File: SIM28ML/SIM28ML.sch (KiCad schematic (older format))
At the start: 26 parts, among them IC1 SIM28M, J1 Conn_01x05, J2 Conn_01x05, U2 AP7365-W-7

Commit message: Part Numbers Added
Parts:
- AE1: Part (none) -> C88374
- BT1: Part (none) -> C238097
- C1: Part (none) -> C87998
- C2, C6: Part (none) -> C42998
- C3, C4: Part (none) -> C396719
- IC1: Description GPS Receiver -> (none); Height 2 -> (none); Manufacturer_Name SIMCOM -> (none); Manufacturer_Part_Number SIM28M -> (none); Part (none) -> OTTO
- L1: Part (none) -> C142204
- R1, R2: Part (none) -> C245184
- R3: Part (none) -> C99198
- R4: Part (none) -> C269698
- R5: Part (none) -> C176153
- R7: Part (none) -> C163436
- R8: Part (none) -> C103426
- U2: Part (none) -> C264087
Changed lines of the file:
@@
 EESchema Schematic File Version 4
-LIBS:SIM28M-cache
+LIBS:SIM28ML-cache
 EELAYER 29 0
 EELAYER END
@@
 F 2 "Package_TO_SOT_SMD:SOT-23-5" H 2450 1675 50  0001 C CNN
 F 3 "https://www.diodes.com/assets/Datasheets/AP2127.pdf" H 2450 1450 50  0001 C CNN
+F 4 "C264087" H 2450 1350 50  0001 C CNN "Part"
 	1    2450 1350
 	1    0    0    -1
@@
 F 2 "Resistor_SMD:R_0603_1608Metric" V 3040 1240 50  0001 C CNN
 F 3 "~" H 3000 1250 50  0001 C CNN
+F 4 "C163436" V 3000 1250 50  0001 C CNN "Part"
 	1    3000 1250
 	0    -1   -1   0
@@
 F 2 "Resistor_SMD:R_0603_1608Metric" V 3240 1540 50  0001 C CNN
 F 3 "~" H 3200 1550 50  0001 C CNN
+F 4 "C103426" H 3200 1550 50  0001 C CNN "Part"
 	1    3200 1550
 	-1   0    0    1
@@
 F 2 "SirBoardLibrary:SIM28M" H 4150 2750 50  0001 L CNN
 F 3 "http://simcomm2m.com/UploadFile/TechnicalFile/SIM28M_Hardware%20Design_V1.00.pdf" H 4150 2650 50  0001 L CNN
-F 4 "GPS Receiver" H 4150 2550 50  0001 L CNN "Description"
-F 5 "2" H 4150 2450 50  0001 L CNN "Height"
-F 6 "SIMCOM" H 4150 2350 50  0001 L CNN "Manufacturer_Name"
-F 7 "SIM28M" H 4150 2250 50  0001 L CNN "Manufacturer_Part_Number"
-F 8 "" H 4150 2150 50  0001 L CNN "Mouser Part Number"
-F 9 "" H 4150 2050 50  0001 L CNN "Mouser Price/Stock"
-F 10 "" H 4150 1950 50  0001 L CNN "RS Part Number"
-F 11 "" H 4150 1850 50  0001 L CNN "RS Price/Stock"
+F 4 "OTTO" H 2800 2650 50  0001 C CNN "Part"
 	1    2800 2650
 	1    0    0    -1
@@
 F 2 "Resistor_SMD:R_0603_1608Metric" V 2290 2840 50  0001 C CNN
 F 3 "~" H 2250 2850 50  0001 C CNN
+F 4 "C245184" V 2250 2850 50  0001 C CNN "Part"
 	1    2250 2850
 	0    -1   1    0
@@
 F 2 "Resistor_SMD:R_0603_1608Metric" V 5140 3340 50  0001 C CNN
 F 3 "~" H 5100 3350 50  0001 C CNN
+F 4 "C269698" V 5100 3350 50  0001 C CNN "Part"
 	1    5100 3350
 	0    -1   1    0
@@
 F 2 "Resistor_SMD:R_0603_1608Metric" V 5140 3040 50  0001 C CNN
 F 3 "~" H 5100 3050 50  0001 C CNN
+F 4 "C176153" V 5100 3050 50  0001 C CNN "Part"
 	1    5100 3050
 	0    -1   1    0
@@
 F 2 "Resistor_SMD:R_0603_1608Metric" V 2290 2740 50  0001 C CNN
 F 3 "~" H 2250 2750 50  0001 C CNN
+F 4 "C245184" V 2250 2750 50  0001 C CNN "Part"
 	1    2250 2750
 	0    -1   -1   0
@@
 F 2 "Battery:BatteryHolder_Keystone_3000_1x12mm" V 2650 3810 50  0001 C CNN
 F 3 "~" V 2650 3810 50  0001 C CNN
+F 4 "C238097" H 2650 3750 50  0001 C CNN "Part"
 	1    2650 3750
 	-1   0    0    -1
@@
 F 2 "Capacitor_SMD:C_0805_2012Metric" H 1488 3450 50  0001 C CNN
 F 3 "~" H 1450 3600 50  0001 C CNN
+F 4 "C87998" H 1450 3600 50  0001 C CNN "Part"
 	1    1450 3600
 	1    0    0    -1
@@
 F 2 "Capacitor_SMD:C_0603_1608Metric" H 1838 3450 50  0001 C CNN
 F 3 "~" H 1800 3600 50  0001 C CNN
+F 4 "C42998" H 1800 3600 50  0001 C CNN "Part"
 	1    1800 3600
 	1    0    0    -1
@@
 F 2 "Inductor_SMD:L_0603_1608Metric" H 5650 3050 50  0001 C CNN
 F 3 "~" H 5650 3050 50  0001 C CNN
+F 4 "C142204" V 5650 3050 50  0001 C CNN "Part"
 	1    5650 3050
 	0    1    -1   0
@@
 F 2 "Capacitor_SMD:C_0603_1608Metric" H 4838 2650 50  0001 C CNN
 F 3 "~" H 4800 2800 50  0001 C CNN
+F 4 "C42998" H 4800 2800 50  0001 C CNN "Part"
 	1    4800 2800
 	1    0    0    1
@@
 F 2 "Connector_Coaxial:U.FL_Hirose_U.FL-R-SMT-1_Vertical" H 6200 2950 50  0001 C CNN
 F 3 "~" H 6200 2950 50  0001 C CNN
+F 4 "C88374" H 6200 2850 50  0001 C CNN "Part"
 	1    6200 2850
 	1    0    0    -1
@@
 F 2 "Capacitor_SMD:C_0805_2012Metric" H 1588 1400 50  0001 C CNN
 F 3 "~" H 1550 1550 50  0001 C CNN
+F 4 "C396719" H 1550 1550 50  0001 C CNN "Part"
 	1    1550 1550
 	1    0    0    -1
@@
 F 2 "Resistor_SMD:R_0603_1608Metric" V 1890 1340 50  0001 C CNN
 F 3 "~" H 1850 1350 50  0001 C CNN
+F 4 "C99198" V 1850 1350 50  0001 C CNN "Part"
 	1    1850 1350
 	0    -1   1    0
@@
 F 2 "Capacitor_SMD:C_0805_2012Metric" H 3488 1400 50  0001 C CNN
 F 3 "~" H 3450 1550 50  0001 C CNN
+F 4 "C396719" H 3450 1550 50  0001 C CNN "Part"
 	1    3450 1550
 	1    0    0    -1

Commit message: Power LED added
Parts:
- removed R7: 68K, Resistor_SMD:R_0603_1608Metric, symbol Device:R_US
- removed R8: 22K, Resistor_SMD:R_0603_1608Metric, symbol Device:R_US
- removed U2: AP7365-W-7, Package_TO_SOT_SMD:SOT-23-5, symbol Regulator_Linear:AP2127K-ADJ
- added D1: LED, LED_SMD:LED_0603_1608Metric, symbol Device:LED
- added JP2: SolderJumper_2_Bridged, Jumper:SolderJumper-2_P1.3mm_Bridged_RoundedPad1.0x1.5mm, symbol Jumper:SolderJumper_2_Bridged
- added R6: 680E, Resistor_SMD:R_0603_1608Metric, symbol Device:R_US
- added U1: AP2127K-3.3, Package_TO_SOT_SMD:SOT-23-5, symbol Regulator_Linear:AP2127K-3.3
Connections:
- wire segments 85 -> 82
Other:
- moved on the sheet: C3, C4, R3
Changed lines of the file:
@@
 Comment4 ""
 $EndDescr
-Text GLabel 3600 1100 2    50   Input ~ 0
+Text GLabel 3300 925  2    50   Input ~ 0
 3V3
 Wire Wire Line
-	1550 1400 1550 1350
-Wire Wire Line
-	1550 1700 1550 1850
+	1275 1300 1275 1025
+Wire Wire Line
+	1275 1600 1275 1925
 $Comp
 L power:GND #PWR0103
 U 1 1 5DFA7870
-P 2450 1950
-F 0 "#PWR0103" H 2450 1700 50  0001 C CNN
-F 1 "GND" H 2455 1777 50  0000 C CNN
-F 2 "" H 2450 1950 50  0001 C CNN
-F 3 "" H 2450 1950 50  0001 C CNN
-	1    2450 1950
-	1    0    0    -1
-$EndComp
-$Comp
-L Regulator_Linear:AP2127K-ADJ U2
-U 1 1 5E2BA0AD
-P 2450 1350
-F 0 "U2" H 2450 1690 50  0000 C CNN
-F 1 "AP7365-W-7" H 2450 1600 50  0000 C CNN
-F 2 "Package_TO_SOT_SMD:SOT-23-5" H 2450 1675 50  0001 C CNN
-F 3 "https://www.diodes.com/assets/Datasheets/AP2127.pdf" H 2450 1450 50  0001 C CNN
-F 4 "C264087" H 2450 1350 50  0001 C CNN "Part"
-	1    2450 1350
-	1    0    0    -1
-$EndComp
-$Comp
-L Device:R_US R7
-U 1 1 5E34715F
-P 3000 1250
-F 0 "R7" V 3068 1296 50  0000 L CNN
-F 1 "68K" V 3068 1205 50  0000 R CNN
-F 2 "Resistor_SMD:R_0603_1608Metric" V 3040 1240 50  0001 C CNN
-F 3 "~" H 3000 1250 50  0001 C CNN
-F 4 "C163436" V 3000 1250 50  0001 C CNN "Part"
-	1    3000 1250
-	0    -1   -1   0
-$EndComp
-$Comp
-L Device:R_US R8
-U 1 1 5E35753D
-P 3200 1550
-F 0 "R8" H 3300 1500 50  0000 L CNN
-F 1 "22K" H 3400 1600 50  0000 R CNN
-F 2 "Resistor_SMD:R_0603_1608Metric" V 3240 1540 50  0001 C CNN
-F 3 "~" H 3200 1550 50  0001 C CNN
-F 4 "C103426" H 3200 1550 50  0001 C CNN "Part"
-	1    3200 1550
-	-1   0    0    1
-$EndComp
-Wire Wire Line
-	3200 1350 2750 1350
-Wire Wire Line
-	3150 1250 3200 1250
-Wire Wire Line
-	3200 1400 3200 1350
+P 2175 2025
+F 0 "#PWR0103" H 2175 1775 50  0001 C CNN
+F 1 "GND" H 2180 1852 50  0000 C CNN
+F 2 "" H 2175 2025 50  0001 C CNN
+F 3 "" H 2175 2025 50  0001 C CNN
+	1    2175 2025
+	1    0    0    -1
+$EndComp
 $Comp
 L SIM28M:SIM28M IC1
@@
 Connection ~ 1450 3350
 Wire Wire Line
-	1550 1850 2450 1850
-Wire Wire Line
-	3200 1700 3200 1850
-Wire Wire Line
-	3200 1350 3200 1250
-Connection ~ 3200 1350
-Wire Wire Line
-	2750 1250 2800 1250
-Wire Wire Line
-	2800 1250 2800 1100
-Connection ~ 2800 1250
-Wire Wire Line
-	2800 1250 2850 1250
-Wire Wire Line
-	2800 1100 3450 1100
+	1275 1925 2175 1925
 $Comp
 L Device:C C3
 U 1 1 5DCB3070
-P 1550 1550
-F 0 "C3" H 1665 1595 50  0000 L CNN
-F 1 "1uF" H 1665 1505 50  0000 L CNN
-F 2 "Capacitor_SMD:C_0805_2012Metric" H 1588 1400 50  0001 C CNN
-F 3 "~" H 1550 1550 50  0001 C CNN
-F 4 "C396719" H 1550 1550 50  0001 C CNN "Part"
-	1    1550 1550
-	1    0    0    -1
-$EndComp
-Wire Wire Line
-	3450 1400 3450 1100
-Connection ~ 3450 1100
-Wire Wire Line
-	3450 1100 3600 1100
-Wire Wire Line
-	3450 1700 3450 1850
-Wire Wire Line
-	3450 1850 3200 1850
-Connection ~ 3200 1850
-Text GLabel 1300 1250 0    50   Input ~ 0
+P 1275 1450
+F 0 "C3" H 1390 1495 50  0000 L CNN
+F 1 "1uF" H 1390 1405 50  0000 L CNN
+F 2 "Capacitor_SMD:C_0805_2012Metric" H 1313 1300 50  0001 C CNN
+F 3 "~" H 1275 1450 50  0001 C CNN
+F 4 "C396719" H 1275 1450 50  0001 C CNN "Part"
+	1    1275 1450
+	1    0    0    -1
+$EndComp
+Text GLabel 1025 925  0    50   Input ~ 0
 VIN
 Wire Wire Line
-	1300 1250 1550 1250
-Connection ~ 1550 1250
+	1025 925  1275 925
+Connection ~ 1275 925
 Text GLabel 4500 2000 0    50   Input ~ 0
 3V3
@@
 VIN
 Wire Wire Line
-	1550 1250 2150 1250
+	1275 925  1875 925
 $Comp
 L Device:R_US R3
 U 1 1 5DCC87E2
-P 1850 1350
-F 0 "R3" V 1918 1396 50  0000 L CNN
-F 1 "10K" V 1918 1305 50  0000 R CNN
-F 2 "Resistor_SMD:R_0603_1608Metric" V 1890 1340 50  0001 C CNN
-F 3 "~" H 1850 1350 50  0001 C CNN
-F 4 "C99198" V 1850 1350 50  0001 C CNN "Part"
-	1    1850 1350
+P 1575 1025
+F 0 "R3" V 1643 1071 50  0000 L CNN
+F 1 "10K" V 1643 980 50  0000 R CNN
+F 2 "Resistor_SMD:R_0603_1608Metric" V 1615 1015 50  0001 C CNN
+F 3 "~" H 1575 1025 50  0001 C CNN
+F 4 "C99198" V 1575 1025 50  0001 C CNN "Part"
+	1    1575 1025
 	0    -1   1    0
 $EndComp
 Wire Wire Line
-	2000 1350 2100 1350
-Wire Wire Line
-	1700 1350 1550 1350
-Connection ~ 1550 1350
-Wire Wire Line
-	1550 1350 1550 1250
-Text GLabel 2050 1550 0    50   Input ~ 0
-EN
-Wire Wire Line
-	2050 1550 2100 1550
-Wire Wire Line
-	2100 1550 2100 1350
-Connection ~ 2100 1350
-Wire Wire Line
-	2100 1350 2150 1350
-$Comp
-L Device:C C4
-U 1 1 5DB8E885
-P 3450 1550
-F 0 "C4" H 3565 1595 50  0000 L CNN
-F 1 "1uF" H 3565 1505 50  0000 L CNN
-F 2 "Capacitor_SMD:C_0805_2012Metric" H 3488 1400 50  0001 C CNN
-F 3 "~" H 3450 1550 50  0001 C CNN
-F 4 "C396719" H 3450 1550 50  0001 C CNN "Part"
-	1    3450 1550
-	1    0    0    -1
-$EndComp
+	1725 1025 1825 1025
+Wire Wire Line
+	1425 1025 1275 1025
+Connection ~ 1275 1025
+Wire Wire Line
+	1275 1025 1275 925
+Connection ~ 1825 1025
+Wire Wire Line
+	1825 1025 1875 1025
 $Comp
 L Mechanical:MountingHole H1
@@
 $EndComp
 Wire Wire Line
-	2450 1650 2450 1850
-Connection ~ 2450 1850
-Wire Wire Line
-	2450 1850 3200 1850
-Wire Wire Line
-	2450 1850 2450 1950
+	2175 1325 2175 1925
+Connection ~ 2175 1925
+Wire Wire Line
+	2175 1925 2175 2025
 $Comp
 L Connector_Generic:Conn_01x05 J1
@@
 Wire Wire Line
 	4650 3250 4650 3900
+$Comp
+L Regulator_Linear:AP2127K-3.3 U1
+U 1 1 5DF815E8
+P 2175 1025
+F 0 "U1" H 2175 1365 50  0000 C CNN
+F 1 "AP2127K-3.3" H 2175 1275 50  0000 C CNN
+F 2 "Package_TO_SOT_SMD:SOT-23-5" H 2175 1350 50  0001 C CNN
+F 3 "https://www.diodes.com/assets/Datasheets/AP2127.pdf" H 2175 1125 50  0001 C CNN
+	1    2175 1025
+	1    0    0    -1
+$EndComp
+Wire Wire Line
+	2175 1925 2775 1925
+$Comp
+L Device:C C4
+U 1 1 5DB8E885
+P 2775 1400
+F 0 "C4" H 2890 1445 50  0000 L CNN
+F 1 "1uF" H 2890 1355 50  0000 L CNN
+F 2 "Capacitor_SMD:C_0805_2012Metric" H 2813 1250 50  0001 C CNN
+F 3 "~" H 2775 1400 50  0001 C CNN
+F 4 "C396719" H 2775 1400 50  0001 C CNN "Part"
+	1    2775 1400
+	1    0    0    -1
+$EndComp
+Wire Wire Line
+	2775 1550 2775 1925
+Wire Wire Line
+	2775 1250 2775 925
+Wire Wire Line
+	2475 925  2775 925
+Wire Wire Line
+	1825 1225 1825 1025
+Wire Wire Line
+	1775 1225 1825 1225
+Text GLabel 1775 1225 0    50   Input ~ 0
+EN
+Connection ~ 2775 925
+Wire Wire Line
+	2775 925  3175 925
+Connection ~ 2775 1925
+Wire Wire Line
+	2775 1925 3175 1925
+$Comp
+L Device:R_US R6
+U 1 1 5DFAD977
+P 3175 1425
+F 0 "R6" H 3250 1375 50  0000 L CNN
+F 1 "680E" H 3250 1475 50  0000 L CNN
+F 2 "Resistor_SMD:R_0603_1608Metric" V 3215 1415 50  0001 C CNN
+F 3 "~" H 3175 1425 50  0001 C CNN
+F 4 "C269441" V 3175 1425 50  0001 C CNN "Part"
+	1    3175 1425
+	1    0    0    1
+$EndComp
+$Comp
+L Device:LED D1
+U 1 1 5DFB00AA
+P 3175 1750
+F 0 "D1" V 3213 1632 50  0000 R CNN
+F 1 "LED" V 3123 1632 50  0000 R CNN
+F 2 "LED_SMD:LED_0603_1608Metric" H 3175 1750 50  0001 C CNN
+F 3 "~" H 3175 1750 50  0001 C CNN
+F 4 "C193191" V 3175 1750 50  0001 C CNN "Part"
+	1    3175 1750
+	0    -1   -1   0
+$EndComp
+Wire Wire Line
+	3175 1900 3175 1925
+Wire Wire Line
+	3175 1600 3175 1575
+$Comp
+L Jumper:SolderJumper_2_Bridged JP2
+U 1 1 5DFB467A
+P 3175 1100
+F 0 "JP2" V 3130 1168 50  0000 L CNN
+F 1 "SolderJumper_2_Bridged" V 3220 1168 50  0000 L CNN
+F 2 "Jumper:SolderJumper-2_P1.3mm_Bridged_RoundedPad1.0x1.5mm" H 3175 1100 50  0001 C CNN
+F 3 "~" H 3175 1100 50  0001 C CNN
+	1    3175 1100
+	0    1    1    0
+$EndComp
+Wire Wire Line
+	3175 1250 3175 1275
+Wire Wire Line
+	3175 950  3175 925
+Connection ~ 3175 925
+Wire Wire Line
+	3175 925  3300 925
 $EndSCHEMATC

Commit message: Schematic PDF and 3D Renders added
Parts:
- IC1: symbol SIM28M:SIM28M -> SIM28ML-rescue:SIM28M-SIM28M
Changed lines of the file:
@@
 $EndComp
 $Comp
-L SIM28M:SIM28M IC1
+L SIM28ML-rescue:SIM28M-SIM28M IC1
 U 1 1 5DC84452
 P 2800 2650

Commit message: Board Sizes Updated
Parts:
- H1, H2, H3, H4: footprint MountingHole:MountingHole_2.7mm_M2.5_ISO14580_Pad -> SirBoardLibrary:MountingHole_M2.5_SirBoard
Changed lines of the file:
@@
 F 0 "H1" H 5750 1850 50  0000 L CNN
 F 1 "MountingHole" H 5750 1805 50  0001 L CNN
-F 2 "MountingHole:MountingHole_2.7mm_M2.5_ISO14580_Pad" H 5650 1850 50  0001 C CNN
+F 2 "SirBoardLibrary:MountingHole_M2.5_SirBoard" H 5650 1850 50  0001 C CNN
 F 3 "~" H 5650 1850 50  0001 C CNN
 	1    5650 1850
@@
 F 0 "H2" H 6400 1850 50  0000 L CNN
 F 1 "MountingHole" H 6400 1805 50  0001 L CNN
-F 2 "MountingHole:MountingHole_2.7mm_M2.5_ISO14580_Pad" H 6300 1850 50  0001 C CNN
+F 2 "SirBoardLibrary:MountingHole_M2.5_SirBoard" H 6300 1850 50  0001 C CNN
 F 3 "~" H 6300 1850 50  0001 C CNN
 	1    6300 1850
@@
 F 0 "H3" H 5750 1250 50  0000 L CNN
 F 1 "MountingHole" H 5750 1205 50  0001 L CNN
-F 2 "MountingHole:MountingHole_2.7mm_M2.5_ISO14580_Pad" H 5650 1250 50  0001 C CNN
+F 2 "SirBoardLibrary:MountingHole_M2.5_SirBoard" H 5650 1250 50  0001 C CNN
 F 3 "~" H 5650 1250 50  0001 C CNN
 	1    5650 1250
@@
 F 0 "H4" H 6400 1250 50  0000 L CNN
 F 1 "MountingHole" H 6400 1205 50  0001 L CNN
-F 2 "MountingHole:MountingHole_2.7mm_M2.5_ISO14580_Pad" H 6300 1250 50  0001 C CNN
+F 2 "SirBoardLibrary:MountingHole_M2.5_SirBoard" H 6300 1250 50  0001 C CNN
 F 3 "~" H 6300 1250 50  0001 C CNN
 	1    6300 1250

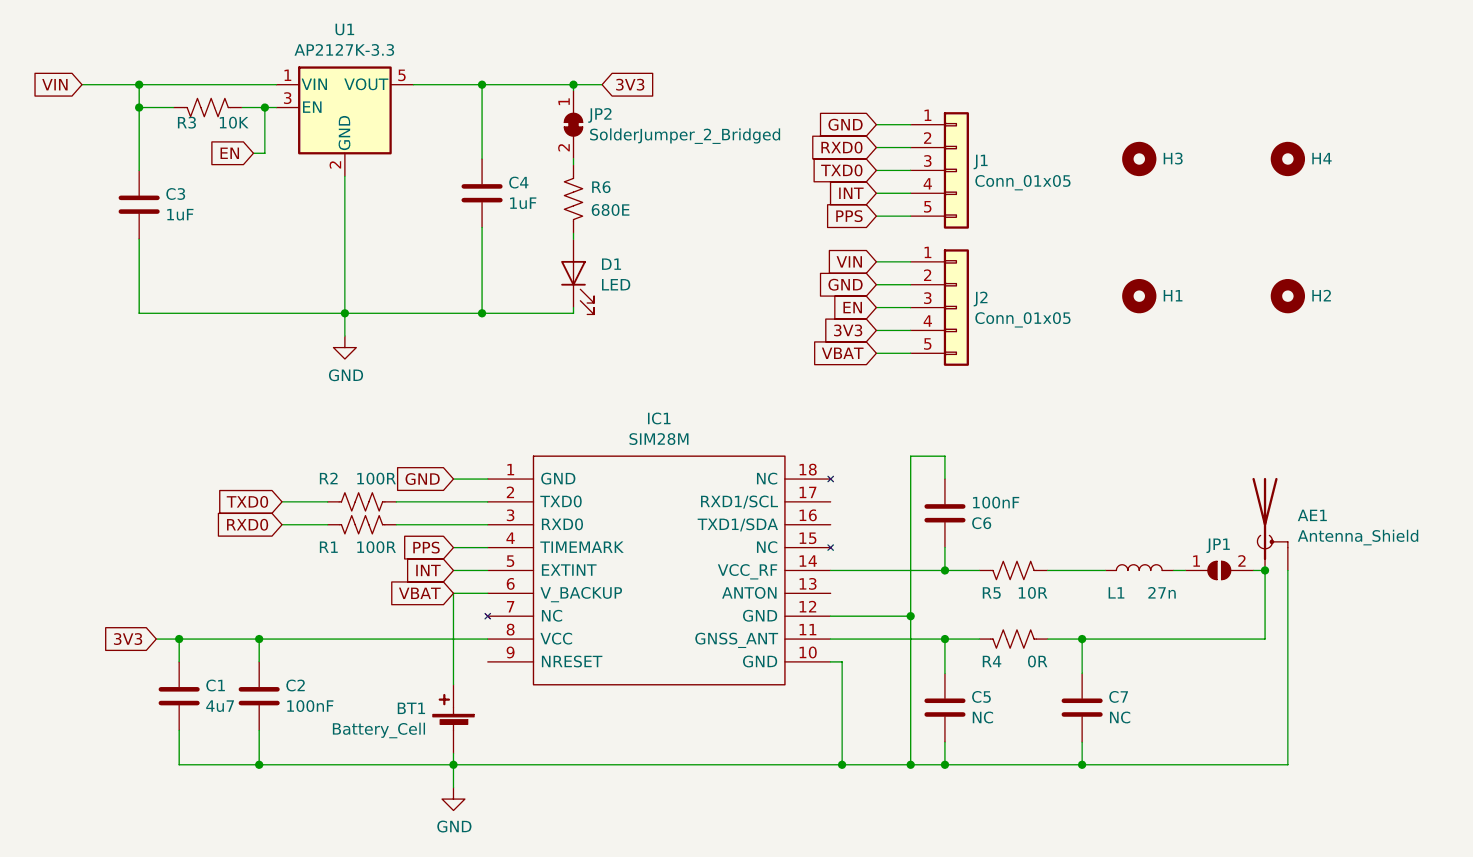
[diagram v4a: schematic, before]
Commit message: SIM28ML Revision2
Active Antenna components removed, Battery connector changed
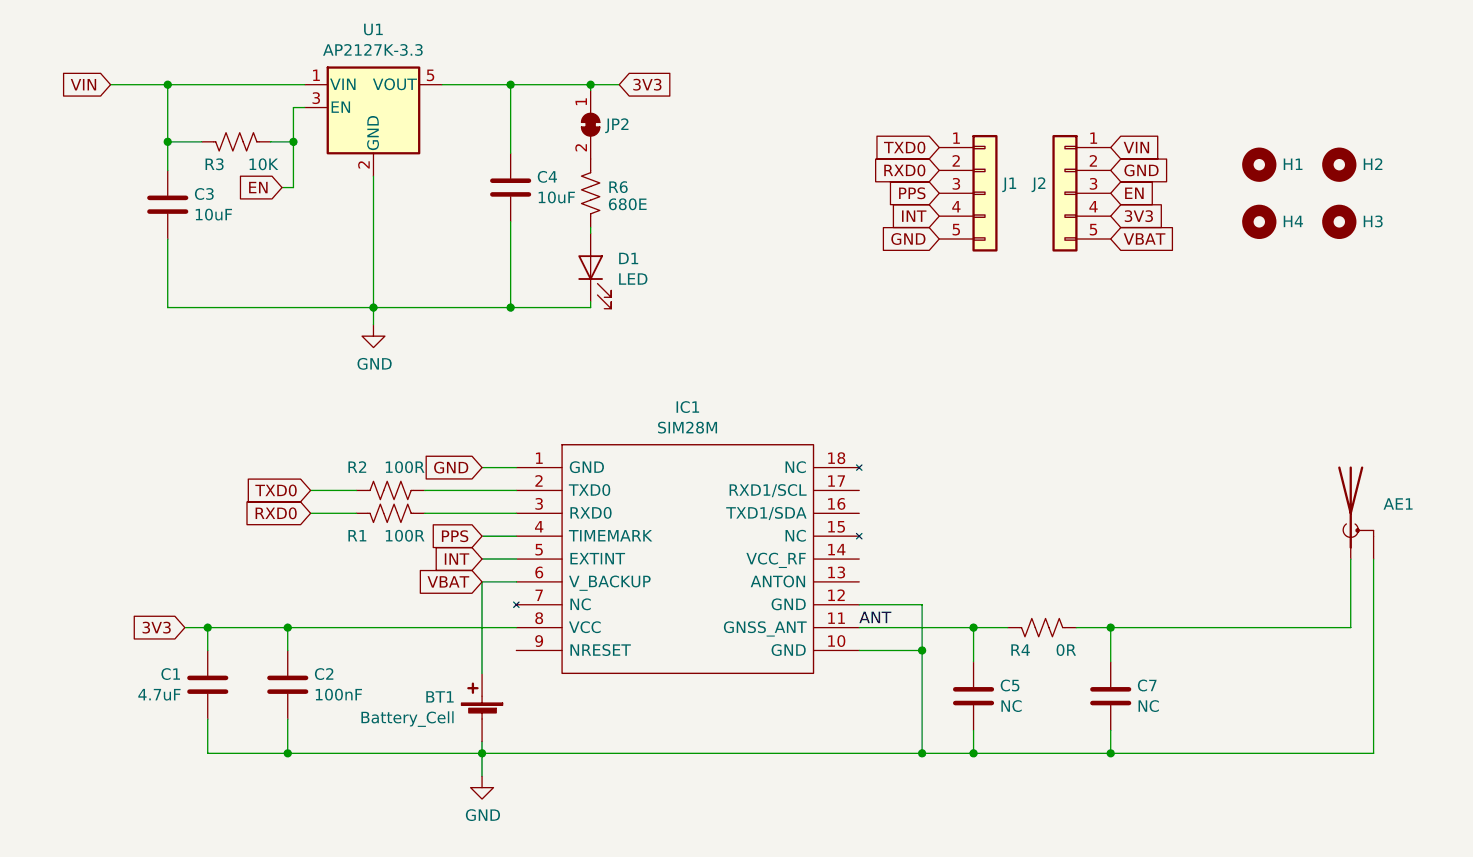
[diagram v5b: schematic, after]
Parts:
- removed C6: 100nF, Capacitor_SMD:C_0603_1608Metric, symbol Device:C
- removed IC1: SIM28M, SirBoardLibrary:SIM28M, symbol SIM28ML-rescue:SIM28M-SIM28M
- removed JP1: SolderJumper_2_Open, Jumper:SolderJumper-2_P1.3mm_Open_RoundedPad1.0x1.5mm, symbol Jumper:SolderJumper_2_Open
- removed L1: 27n, Inductor_SMD:L_0603_1608Metric, symbol Device:L
- removed R5: 10R, Resistor_SMD:R_0603_1608Metric, symbol Device:R_US
- added IC1: SIM28M, SIM28M, symbol SirBoard_Library:SIM28M
- BT1: footprint Battery:BatteryHolder_Keystone_3000_1x12mm -> SirBoardLibrary:S8411-45R_1; Part C238097 -> C70381
- C1: value 4u7 -> 4.7uF; footprint Capacitor_SMD:C_0805_2012Metric -> Capacitor_SMD:C_0603_1608Metric; Part C87998 -> (none)
- C3, C4: value 1uF -> 10uF; Part C396719 -> C95841
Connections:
- net 3V3: now also IC1.8 (VCC)
- net GND: now also J1.5 (Pin_5), IC1.1 (GND), IC1.10 (GND), IC1.12 (GND); no longer J1.1 (Pin_1)
- net INT: now also IC1.5 (EXTINT)
- net PPS: now also J1.3 (Pin_3), IC1.4 (TIMEMARK); no longer J1.5 (Pin_5)
- net TXD0: now also J1.1 (Pin_1); no longer J1.3 (Pin_3)
- net VBAT: now also IC1.6 (V_BACKUP)
- net ANT: now reaches C5.1, R4.1
- net ANT: now also IC1.11 (GNSS_ANT)
- net at R2.2: now also IC1.2 (TXD0)
- net at R1.2: now also IC1.3 (RXD0)
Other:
- moved on the sheet: AE1, BT1, C1, C2, C3, C4, C5, C7, H1, H2, H3, H4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
